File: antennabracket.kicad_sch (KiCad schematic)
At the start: 12 parts, among them J10 Conn_Coaxial, J11 Conn_Coaxial, J12 Conn_Coaxial, J3 Conn_Coaxial, J7 Conn_Coaxial, J8 Conn_Coaxial

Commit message: finished slateconnect i2c gpio expander, completed led status bar schematic, fixed all drc errors, started assigning footprints and started bom
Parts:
- J10, J11, J12, J3, J7, J8: footprint (none) -> Connector_Coaxial:U.FL_Hirose_U.FL-R-SMT-1(10); MPN (none) -> U.FL-R-SMT-1(10); Manufacturer (none) -> Hirose

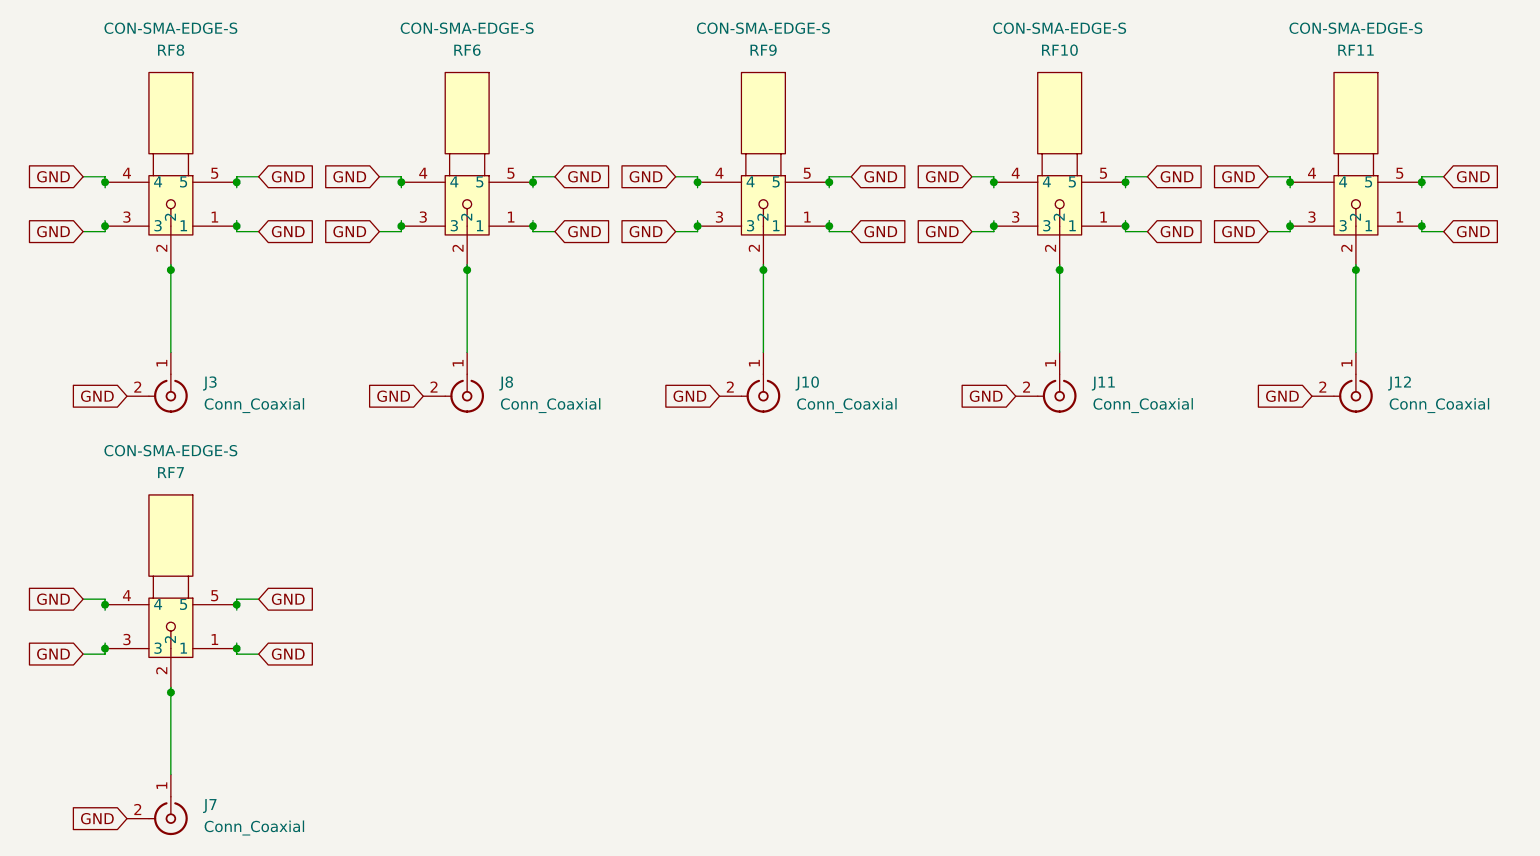
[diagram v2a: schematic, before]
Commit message: finished BOM, replaced discontinued parts, added missing footprints, updated schematics and libraries
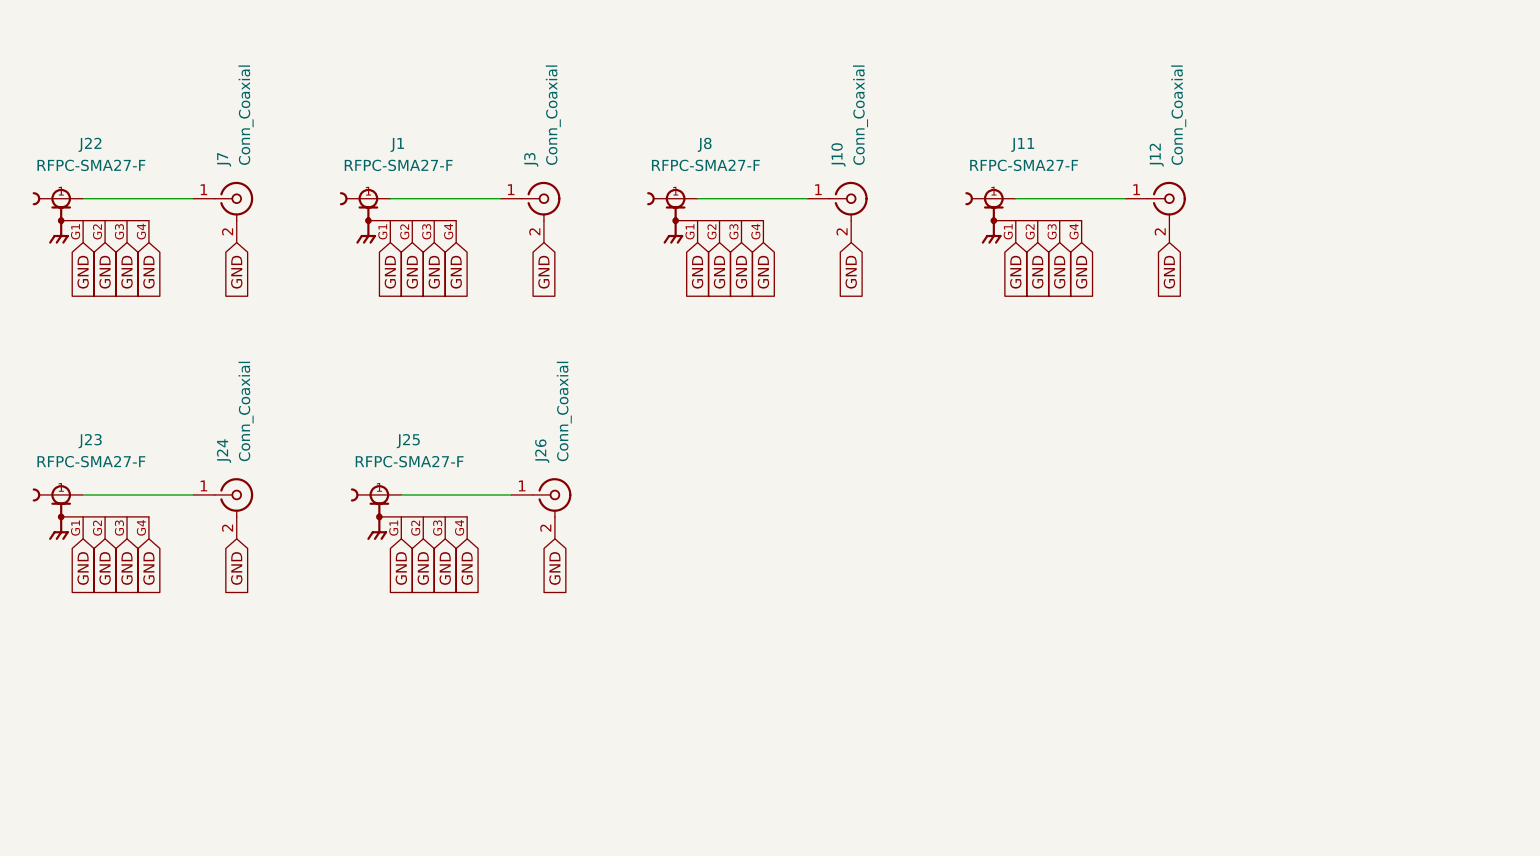
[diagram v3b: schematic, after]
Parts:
- removed J11, J8: Conn_Coaxial, Connector_Coaxial:U.FL_Hirose_U.FL-R-SMT-1(10), symbol Connector:Conn_Coaxial
- removed RF10, RF11, RF6, RF7, RF8, RF9: CON-SMA-EDGE-S, slate113:SMA-SMD_CON-SMA-EDGE-S, symbol slate113:CON-SMA-EDGE-S
- added J1, J8: RFPC-SMA27-F, RFPC-SMA27-F:GRADCONN_RFPC-SMA27-F, symbol slate113:RFPC-SMA27-F
- added J11, J22, J23, J25: RFPC-SMA27-F, slate113:GRADCONN_RFPC-SMA27-F, symbol slate113:RFPC-SMA27-F
- added J24, J26: Conn_Coaxial, Connector_Coaxial:U.FL_Hirose_U.FL-R-SMT-1(10), symbol Connector:Conn_Coaxial
- J10, J12, J3, J7: LCSC Part (none) -> C496552; MPN U.FL-R-SMT-1(10) -> BWIPX-1-001E; Manufacturer Hirose -> IPEX
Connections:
- net GND: now also J1.G1, J1.G2, J1.G3, J1.G4, J11.G1, J11.G2, J11.G3, J11.G4, J22.G1, J22.G2, J22.G3, J22.G4, J23.G1, J23.G2, J23.G3, J23.G4, J24.2 (Ext), J25.G1, J25.G2, J25.G3, J25.G4, J26.2 (Ext), J8.G1, J8.G2, J8.G3, J8.G4
- net at J12.1 (In): now also J11.1
- net at J3.1 (In): now also J1.1
- net at J10.1 (In): now also J8.1
- net at J7.1 (In): now also J22.1
- new net: J23.1, J24.1 (In)
- new net: J25.1, J26.1 (In)
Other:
- moved on the sheet: J7

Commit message: imported footprints and 3d models, replaced obsolete components, finished schematic audit, wired new usb hub and flash chip + more, removed stale nets
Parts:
- J1, J8: DigiKey Part (none) -> 2073-RFPC-SMA27-F-ND; MPN (none) -> RFPC-SMA27-F; Manufacturer (none) -> GCT
- J11, J22, J23, J25: footprint slate113:GRADCONN_RFPC-SMA27-F -> RFPC-SMA27-F:GRADCONN_RFPC-SMA27-F; DigiKey Part (none) -> 2073-RFPC-SMA27-F-ND; MPN (none) -> RFPC-SMA27-F; Manufacturer (none) -> GCT
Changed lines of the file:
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@@
 			)
 		)
-		(property "Datasheet" ""
+		(property "Datasheet" "https://www.mouser.com/datasheet/2/837/RFPC_SMA27_F-3511583.pdf"
 			(at 57.15 41.91 0)
 			(hide yes)
@@
 				)
 				(justify bottom)
+			)
+		)
+		(property "MPN" "RFPC-SMA27-F"
+			(at 0 0 0)
+			(hide yes)
+			(show_name no)
+			(do_not_autoplace no)
+			(effects
+				(font
+					(size 1.27 1.27)
+				)
+			)
+		)
+		(property "Manufacturer" "GCT"
+			(at 0 0 0)
+			(hide yes)
+			(show_name no)
+			(do_not_autoplace no)
+			(effects
+				(font
+					(size 1.27 1.27)
+				)
+			)
+		)
+		(property "DigiKey Part" "2073-RFPC-SMA27-F-ND"
+			(at 0 0 0)
+			(hide yes)
+			(show_name no)
+			(do_not_autoplace no)
+			(effects
+				(font
+					(size 1.27 1.27)
+				)
 			)
 		)
@@
 			)
 		)
-		(property "Datasheet" ""
+		(property "Datasheet" "https://www.mouser.com/datasheet/2/837/RFPC_SMA27_F-3511583.pdf"
 			(at 92.71 41.91 0)
 			(hide yes)
@@
 				)
 				(justify bottom)
+			)
+		)
+		(property "MPN" "RFPC-SMA27-F"
+			(at 0 0 0)
+			(hide yes)
+			(show_name no)
+			(do_not_autoplace no)
+			(effects
+				(font
+					(size 1.27 1.27)
+				)
+			)
+		)
+		(property "Manufacturer" "GCT"
+			(at 0 0 0)
+			(hide yes)
+			(show_name no)
+			(do_not_autoplace no)
+			(effects
+				(font
+					(size 1.27 1.27)
+				)
+			)
+		)
+		(property "DigiKey Part" "2073-RFPC-SMA27-F-ND"
+			(at 0 0 0)
+			(hide yes)
+			(show_name no)
+			(do_not_autoplace no)
+			(effects
+				(font
+					(size 1.27 1.27)
+				)
 			)
 		)
@@
 			)
 		)
-		(property "Footprint" "slate113:GRADCONN_RFPC-SMA27-F"
+		(property "Footprint" "RFPC-SMA27-F:GRADCONN_RFPC-SMA27-F"
 			(at 129.54 41.91 0)
 			(hide yes)
@@
 			)
 		)
-		(property "Datasheet" ""
+		(property "Datasheet" "https://www.mouser.com/datasheet/2/837/RFPC_SMA27_F-3511583.pdf"
 			(at 129.54 41.91 0)
 			(hide yes)
@@
 				)
 				(justify bottom)
+			)
+		)
+		(property "MPN" "RFPC-SMA27-F"
+			(at 0 0 0)
+			(hide yes)
+			(show_name no)
+			(do_not_autoplace no)
+			(effects
+				(font
+					(size 1.27 1.27)
+				)
+			)
+		)
+		(property "Manufacturer" "GCT"
+			(at 0 0 0)
+			(hide yes)
+			(show_name no)
+			(do_not_autoplace no)
+			(effects
+				(font
+					(size 1.27 1.27)
+				)
+			)
+		)
+		(property "DigiKey Part" "2073-RFPC-SMA27-F-ND"
+			(at 0 0 0)
+			(hide yes)
+			(show_name no)
+			(do_not_autoplace no)
+			(effects
+				(font
+					(size 1.27 1.27)
+				)
 			)
 		)
@@
 			)
 		)
-		(property "Footprint" "slate113:GRADCONN_RFPC-SMA27-F"
+		(property "Footprint" "RFPC-SMA27-F:GRADCONN_RFPC-SMA27-F"
 			(at 58.42 76.2 0)
 			(hide yes)
@@
 			)
 		)
-		(property "Datasheet" ""
+		(property "Datasheet" "https://www.mouser.com/datasheet/2/837/RFPC_SMA27_F-3511583.pdf"
 			(at 58.42 76.2 0)
 			(hide yes)
@@
 				)
 				(justify bottom)
+			)
+		)
+		(property "MPN" "RFPC-SMA27-F"
+			(at 0 0 0)
+			(hide yes)
+			(show_name no)
+			(do_not_autoplace no)
+			(effects
+				(font
+					(size 1.27 1.27)
+				)
+			)
+		)
+		(property "Manufacturer" "GCT"
+			(at 0 0 0)
+			(hide yes)
+			(show_name no)
+			(do_not_autoplace no)
+			(effects
+				(font
+					(size 1.27 1.27)
+				)
+			)
+		)
+		(property "DigiKey Part" "2073-RFPC-SMA27-F-ND"
+			(at 0 0 0)
+			(hide yes)
+			(show_name no)
+			(do_not_autoplace no)
+			(effects
+				(font
+					(size 1.27 1.27)
+				)
 			)
 		)
@@
 			)
 		)
-		(property "Footprint" "slate113:GRADCONN_RFPC-SMA27-F"
+		(property "Footprint" "RFPC-SMA27-F:GRADCONN_RFPC-SMA27-F"
 			(at 21.59 76.2 0)
 			(hide yes)
@@
 			)
 		)
-		(property "Datasheet" ""
+		(property "Datasheet" "https://www.mouser.com/datasheet/2/837/RFPC_SMA27_F-3511583.pdf"
 			(at 21.59 76.2 0)
 			(hide yes)
@@
 				)
 				(justify bottom)
+			)
+		)
+		(property "MPN" "RFPC-SMA27-F"
+			(at 0 0 0)
+			(hide yes)
+			(show_name no)
+			(do_not_autoplace no)
+			(effects
+				(font
+					(size 1.27 1.27)
+				)
+			)
+		)
+		(property "Manufacturer" "GCT"
+			(at 0 0 0)
+			(hide yes)
+			(show_name no)
+			(do_not_autoplace no)
+			(effects
+				(font
+					(size 1.27 1.27)
+				)
+			)
+		)
+		(property "DigiKey Part" "2073-RFPC-SMA27-F-ND"
+			(at 0 0 0)
+			(hide yes)
+			(show_name no)
+			(do_not_autoplace no)
+			(effects
+				(font
+					(size 1.27 1.27)
+				)
 			)
 		)
@@
 			)
 		)
-		(property "Footprint" "slate113:GRADCONN_RFPC-SMA27-F"
+		(property "Footprint" "RFPC-SMA27-F:GRADCONN_RFPC-SMA27-F"
 			(at 21.59 41.91 0)
 			(hide yes)
@@
 			)
 		)
-		(property "Datasheet" ""
+		(property "Datasheet" "https://www.mouser.com/datasheet/2/837/RFPC_SMA27_F-3511583.pdf"
 			(at 21.59 41.91 0)
 			(hide yes)
@@
 			)
 		)
+		(property "MPN" "RFPC-SMA27-F"
+			(at 0 0 0)
+			(hide yes)
+			(show_name no)
+			(do_not_autoplace no)
+			(effects
+				(font
+					(size 1.27 1.27)
+				)
+			)
+		)
+		(property "Manufacturer" "GCT"
+			(at 0 0 0)
+			(hide yes)
+			(show_name no)
+			(do_not_autoplace no)
+			(effects
+				(font
+					(size 1.27 1.27)
+				)
+			)
+		)
+		(property "DigiKey Part" "2073-RFPC-SMA27-F-ND"
+			(at 0 0 0)
+			(hide yes)
+			(show_name no)
+			(do_not_autoplace no)
+			(effects
+				(font
+					(size 1.27 1.27)
+				)
+			)
+		)

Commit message: finished m.2 board and copper pours, completed antenna bracket and power board, finished slateconnect board, reorganized libraries
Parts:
- added R142, R143, R144, R145, R146, R24: 50Ω, Resistor_SMD:R_0402_1005Metric, symbol Device:R_Small
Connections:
- net GND: now also R142.1, R143.1, R144.1, R145.1, R146.1, R24.1
- net at J10.1 (In), J8.1: now also R145.2
- net at J1.1, J3.1 (In): now also R143.2
- net at J23.1, J24.1 (In): now also R142.2
- net at J11.1, J12.1 (In): now also R146.2
- net at J25.1, J26.1 (In): now also R144.2
- net at J22.1, J7.1 (In): now also R24.2
